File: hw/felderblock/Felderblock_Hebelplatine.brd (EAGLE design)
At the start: 50 x 78 mm, 35 parts, among them IC3 MCP23017SP

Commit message: last check
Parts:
- FS1-5, FS2-6, FS3-7, FS4-8: device Jens:DIL6_LARGE -> Jens:DIL6_LANGLOCH
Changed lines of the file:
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@@
 <attribute name="VALUE" x="30.226" y="5.6388" size="1.27" layer="27" ratio="10" rot="R180"/>
 </element>
-<element name="FS1-5" library="Jens" package="DIL6_LARGE" value="" x="15.24" y="70" smashed="yes">
+<element name="FS1-5" library="Jens" package="DIL6_LANGLOCH" value="" x="15.24" y="70" smashed="yes">
 <attribute name="VALUE" x="10.16" y="61.55" size="1.778" layer="27"/>
 </element>
-<element name="FS2-6" library="Jens" package="DIL6_LARGE" value="" x="15.24" y="50" smashed="yes">
+<element name="FS2-6" library="Jens" package="DIL6_LANGLOCH" value="" x="15.24" y="50" smashed="yes">
 <attribute name="VALUE" x="10.16" y="41.55" size="1.778" layer="27"/>
 </element>
-<element name="FS3-7" library="Jens" package="DIL6_LARGE" value="" x="15.24" y="30" smashed="yes">
+<element name="FS3-7" library="Jens" package="DIL6_LANGLOCH" value="" x="15.24" y="30" smashed="yes">
 <attribute name="VALUE" x="10.16" y="21.55" size="1.778" layer="27"/>
 </element>
-<element name="FS4-8" library="Jens" package="DIL6_LARGE" value="" x="15.24" y="10" smashed="yes">
+<element name="FS4-8" library="Jens" package="DIL6_LANGLOCH" value="" x="15.24" y="10" smashed="yes">
 <attribute name="VALUE" x="10.16" y="1.55" size="1.778" layer="27"/>
 </element>

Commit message: last update for mfg
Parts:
- FS1-5, FS2-6, FS3-7, FS4-8: device Jens:DIL6_LANGLOCH -> Jens:DIL6_LARGE
- LED1, LED2, LED3, LED4, LED5, LED6, LED7, LED8: device SparkFun-LED:LED_3MM -> SparkFun-LED:LED3MM
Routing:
- net +5V: track 182.0 -> 158.7 mm
- net FST7: track 26.9 -> 26.3 mm
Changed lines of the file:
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@@
 <attribute name="VALUE" x="39.7002" y="64.643" size="1.778" layer="27" ratio="10" rot="R270"/>
 </element>
-<element name="LED3" library="SparkFun-LED" package="LED_3MM" value="" x="25.4" y="30" smashed="yes">
-<attribute name="PROD_ID" value="DIO-08794" x="25.4" y="30" size="1.778" layer="27" display="off"/>
+<element name="LED3" library="SparkFun-LED" package="LED3MM" value="" x="25.4" y="30" smashed="yes">
 <attribute name="VALUE" x="25.4" y="27.714" size="0.6096" layer="27" font="vector" ratio="20" align="top-center"/>
 </element>
-<element name="LED8" library="SparkFun-LED" package="LED_3MM" value="" x="5.08" y="10" smashed="yes">
-<attribute name="PROD_ID" value="DIO-08794" x="5.08" y="10" size="1.778" layer="27" display="off"/>
+<element name="LED8" library="SparkFun-LED" package="LED3MM" value="" x="5.08" y="10" smashed="yes">
 <attribute name="VALUE" x="5.08" y="7.714" size="0.6096" layer="27" font="vector" ratio="20" align="top-center"/>
 </element>
-<element name="LED4" library="SparkFun-LED" package="LED_3MM" value="" x="25.4" y="10" smashed="yes">
-<attribute name="PROD_ID" value="DIO-08794" x="25.4" y="10" size="1.778" layer="27" display="off"/>
+<element name="LED4" library="SparkFun-LED" package="LED3MM" value="" x="25.4" y="10" smashed="yes">
 <attribute name="VALUE" x="25.4" y="7.714" size="0.6096" layer="27" font="vector" ratio="20" align="top-center"/>
 </element>
-<element name="LED5" library="SparkFun-LED" package="LED_3MM" value="" x="5.08" y="70" smashed="yes">
-<attribute name="PROD_ID" value="DIO-08794" x="5.08" y="70" size="1.778" layer="27" display="off"/>
+<element name="LED5" library="SparkFun-LED" package="LED3MM" value="" x="5.08" y="70" smashed="yes">
 <attribute name="VALUE" x="5.08" y="67.714" size="0.6096" layer="27" font="vector" ratio="20" align="top-center"/>
 </element>
-<element name="LED1" library="SparkFun-LED" package="LED_3MM" value="" x="25.4" y="70" smashed="yes">
-<attribute name="PROD_ID" value="DIO-08794" x="25.4" y="70" size="1.778" layer="27" display="off"/>
+<element name="LED1" library="SparkFun-LED" package="LED3MM" value="" x="25.4" y="70" smashed="yes">
 <attribute name="VALUE" x="25.4" y="67.714" size="0.6096" layer="27" font="vector" ratio="20" align="top-center"/>
 </element>
-<element name="LED6" library="SparkFun-LED" package="LED_3MM" value="" x="5.08" y="50" smashed="yes">
-<attribute name="PROD_ID" value="DIO-08794" x="5.08" y="50" size="1.778" layer="27" display="off"/>
+<element name="LED6" library="SparkFun-LED" package="LED3MM" value="" x="5.08" y="50" smashed="yes">
 <attribute name="VALUE" x="5.08" y="47.714" size="0.6096" layer="27" font="vector" ratio="20" align="top-center"/>
 </element>
-<element name="LED2" library="SparkFun-LED" package="LED_3MM" value="" x="25.4" y="50" smashed="yes">
-<attribute name="PROD_ID" value="DIO-08794" x="25.4" y="50" size="1.778" layer="27" display="off"/>
+<element name="LED2" library="SparkFun-LED" package="LED3MM" value="" x="25.4" y="50" smashed="yes">
 <attribute name="VALUE" x="25.4" y="47.714" size="0.6096" layer="27" font="vector" ratio="20" align="top-center"/>
 </element>
-<element name="LED7" library="SparkFun-LED" package="LED_3MM" value="" x="5.08" y="30" smashed="yes">
-<attribute name="PROD_ID" value="DIO-08794" x="5.08" y="30" size="1.778" layer="27" display="off"/>
+<element name="LED7" library="SparkFun-LED" package="LED3MM" value="" x="5.08" y="30" smashed="yes">
 <attribute name="VALUE" x="5.08" y="27.714" size="0.6096" layer="27" font="vector" ratio="20" align="top-center"/>
 </element>
@@
 <attribute name="VALUE" x="30.226" y="5.6388" size="1.27" layer="27" ratio="10" rot="R180"/>
 </element>
-<element name="FS1-5" library="Jens" package="DIL6_LANGLOCH" value="" x="15.24" y="70" smashed="yes">
+<element name="FS1-5" library="Jens" package="DIL6_LARGE" value="" x="15.24" y="70" smashed="yes">
 <attribute name="VALUE" x="10.16" y="61.55" size="1.778" layer="27"/>
 </element>
-<element name="FS2-6" library="Jens" package="DIL6_LANGLOCH" value="" x="15.24" y="50" smashed="yes">
+<element name="FS2-6" library="Jens" package="DIL6_LARGE" value="" x="15.24" y="50" smashed="yes">
 <attribute name="VALUE" x="10.16" y="41.55" size="1.778" layer="27"/>
 </element>
-<element name="FS3-7" library="Jens" package="DIL6_LANGLOCH" value="" x="15.24" y="30" smashed="yes">
+<element name="FS3-7" library="Jens" package="DIL6_LARGE" value="" x="15.24" y="30" smashed="yes">
 <attribute name="VALUE" x="10.16" y="21.55" size="1.778" layer="27"/>
 </element>
-<element name="FS4-8" library="Jens" package="DIL6_LANGLOCH" value="" x="15.24" y="10" smashed="yes">
+<element name="FS4-8" library="Jens" package="DIL6_LARGE" value="" x="15.24" y="10" smashed="yes">
 <attribute name="VALUE" x="10.16" y="1.55" size="1.778" layer="27"/>
 </element>
@@
 <wire x1="40.9194" y1="16.4592" x2="41.005" y2="16.425" width="0.254" layer="1"/>
 <wire x1="40.9194" y1="25.146" x2="41.005" y2="25.315" width="0.254" layer="1"/>
-<wire x1="37.2364" y1="12.5476" x2="24.0284" y2="12.5476" width="0.254" layer="1"/>
+<wire x1="37.2364" y1="12.5476" x2="24.6634" y2="12.5476" width="0.254" layer="1"/>
 <wire x1="40.9194" y1="16.2306" x2="37.2364" y2="12.5476" width="0.254" layer="1"/>
 <wire x1="40.9194" y1="16.2306" x2="41.005" y2="16.425" width="0.254" layer="1"/>
 <wire x1="40.9194" y1="42.5958" x2="38.4302" y2="45.085" width="0.6096" layer="1"/>
 <wire x1="38.4302" y1="45.085" x2="36.83" y2="45.085" width="0.6096" layer="1"/>
-<wire x1="24.0284" y1="12.5476" x2="24.0284" y2="11.9634" width="0.3048" layer="1"/>
+<wire x1="24.6634" y1="12.5476" x2="24.0284" y2="11.9634" width="0.3048" layer="1"/>
 <wire x1="24.0284" y1="11.9634" x2="22.225" y2="10.16" width="0.3048" layer="1"/>
-<wire x1="22.225" y1="10.16" x2="17.145" y2="10.16" width="0.3048" layer="1"/>
-<wire x1="15.24" y1="72.4" x2="15.24" y2="73.66" width="0.3048" layer="1"/>
-<wire x1="15.24" y1="73.66" x2="17.145" y2="75.565" width="0.3048" layer="1"/>
-<wire x1="17.145" y1="75.565" x2="25.4" y2="75.565" width="0.3048" layer="1"/>
-<wire x1="25.4" y1="75.565" x2="26.035" y2="74.93" width="0.3048" layer="1"/>
-<wire x1="26.035" y1="74.93" x2="26.035" y2="73.66" width="0.3048" layer="1"/>
-<wire x1="26.035" y1="73.66" x2="25.4" y2="73.025" width="0.3048" layer="1"/>
-<wire x1="25.4" y1="73.025" x2="23.495" y2="73.025" width="0.3048" layer="1"/>
-<wire x1="23.495" y1="73.025" x2="22.225" y2="71.755" width="0.3048" layer="1"/>
-<wire x1="22.225" y1="71.755" x2="22.225" y2="64.77" width="0.3048" layer="1"/>
-<wire x1="22.225" y1="64.77" x2="20.955" y2="63.5" width="0.3048" layer="1"/>
-<wire x1="20.955" y1="63.5" x2="15.875" y2="63.5" width="0.3048" layer="1"/>
-<wire x1="15.875" y1="63.5" x2="8.255" y2="55.88" width="0.3048" layer="1"/>
+<wire x1="17.78" y1="65.405" x2="8.255" y2="55.88" width="0.3048" layer="1"/>
 <wire x1="15.24" y1="52.4" x2="15.24" y2="51.435" width="0.3048" layer="1"/>
 <wire x1="15.24" y1="51.435" x2="13.97" y2="50.165" width="0.3048" layer="1"/>
@@
 <wire x1="15.24" y1="34.925" x2="15.24" y2="32.4" width="0.3048" layer="1"/>
 <wire x1="15.24" y1="12.4" x2="15.24" y2="12.065" width="0.3048" layer="1"/>
-<wire x1="15.24" y1="12.065" x2="17.145" y2="10.16" width="0.3048" layer="1"/>
-<wire x1="17.145" y1="10.16" x2="8.255" y2="10.16" width="0.3048" layer="1"/>
+<wire x1="22.225" y1="10.16" x2="15.24" y2="10.16" width="0.3048" layer="1"/>
+<wire x1="15.24" y1="10.16" x2="8.255" y2="10.16" width="0.3048" layer="1"/>
 <wire x1="8.255" y1="10.16" x2="7.62" y2="10.795" width="0.3048" layer="1"/>
 <wire x1="7.62" y1="10.795" x2="7.62" y2="13.335" width="0.3048" layer="1"/>
@@
 <wire x1="12.7" y1="21.59" x2="8.255" y2="26.035" width="0.3048" layer="1"/>
 <wire x1="8.255" y1="26.035" x2="8.255" y2="35.56" width="0.3048" layer="1"/>
+<wire x1="15.24" y1="12.065" x2="15.24" y2="10.16" width="0.4064" layer="1"/>
+<wire x1="17.79" y1="69.85" x2="15.24" y2="72.4" width="0.3048" layer="1"/>
+<wire x1="17.78" y1="65.405" x2="17.78" y2="69.84" width="0.3048" layer="1"/>
+<wire x1="17.78" y1="69.84" x2="17.79" y2="69.85" width="0.3048" layer="1"/>
 </signal>
 <signal name="FST1">
@@
 <wire x1="35.8902" y1="50.0634" x2="36.8046" y2="50.0634" width="0.254" layer="16"/>
 <wire x1="33.3756" y1="47.5488" x2="35.8902" y2="50.0634" width="0.254" layer="16"/>
-<wire x1="33.3756" y1="44.3484" x2="33.3756" y2="47.5488" width="0.254" layer="16"/>
+<wire x1="33.3756" y1="45.6184" x2="33.3756" y2="47.5488" width="0.254" layer="16"/>
 <wire x1="36.8046" y1="50.0634" x2="36.83" y2="50.165" width="0.254" layer="16"/>
 <wire x1="22.5158" y1="34.9758" x2="19.94" y2="32.4" width="0.3048" layer="1"/>
-<wire x1="33.3756" y1="44.3484" x2="32.2834" y2="44.3484" width="0.3048" layer="16"/>
+<wire x1="33.3756" y1="45.6184" x2="32.2834" y2="44.3484" width="0.3048" layer="16"/>
 <wire x1="32.2834" y1="44.3484" x2="24.13" y2="36.195" width="0.3048" layer="16"/>
 <wire x1="24.13" y1="36.195" x2="24.13" y2="34.925" width="0.3048" layer="16"/>
@@
 <wire x1="47.3202" y1="66.0654" x2="47.3202" y2="58.293" width="0.254" layer="1"/>
 <wire x1="45.9486" y1="67.437" x2="47.3202" y2="66.0654" width="0.254" layer="1"/>
-<wire x1="26.9748" y1="67.437" x2="45.9486" y2="67.437" width="0.254" layer="1"/>
-<wire x1="21.9456" y1="62.4078" x2="26.9748" y2="67.437" width="0.254" layer="1"/>
-<wire x1="17.8308" y1="62.4078" x2="21.9456" y2="62.4078" width="0.254" layer="1"/>
+<wire x1="27.6098" y1="67.437" x2="45.9486" y2="67.437" width="0.254" layer="1"/>
+<wire x1="22.5806" y1="62.4078" x2="27.6098" y2="67.437" width="0.254" layer="1"/>
+<wire x1="17.8308" y1="62.4078" x2="22.5806" y2="62.4078" width="0.254" layer="1"/>
 <wire x1="44.577" y1="57.8358" x2="44.45" y2="57.785" width="0.254" layer="1"/>
 <wire x1="17.8308" y1="62.4078" x2="17.78" y2="62.23" width="0.254" layer="1"/>

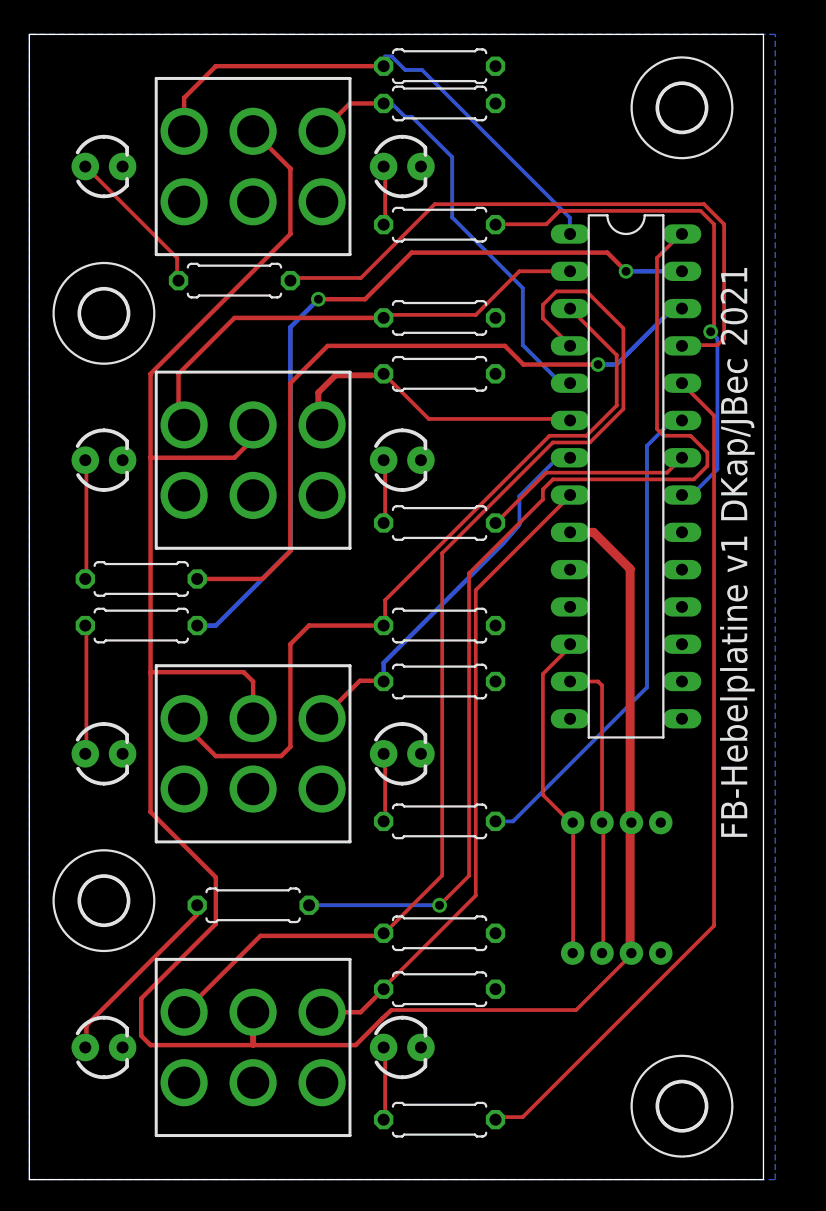
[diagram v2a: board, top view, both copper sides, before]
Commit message: moved components to backside
- Components of main panel moved to backside
-  corrected connections for MCP on Hebelplatine
- added address jumpers on Hebelplatine
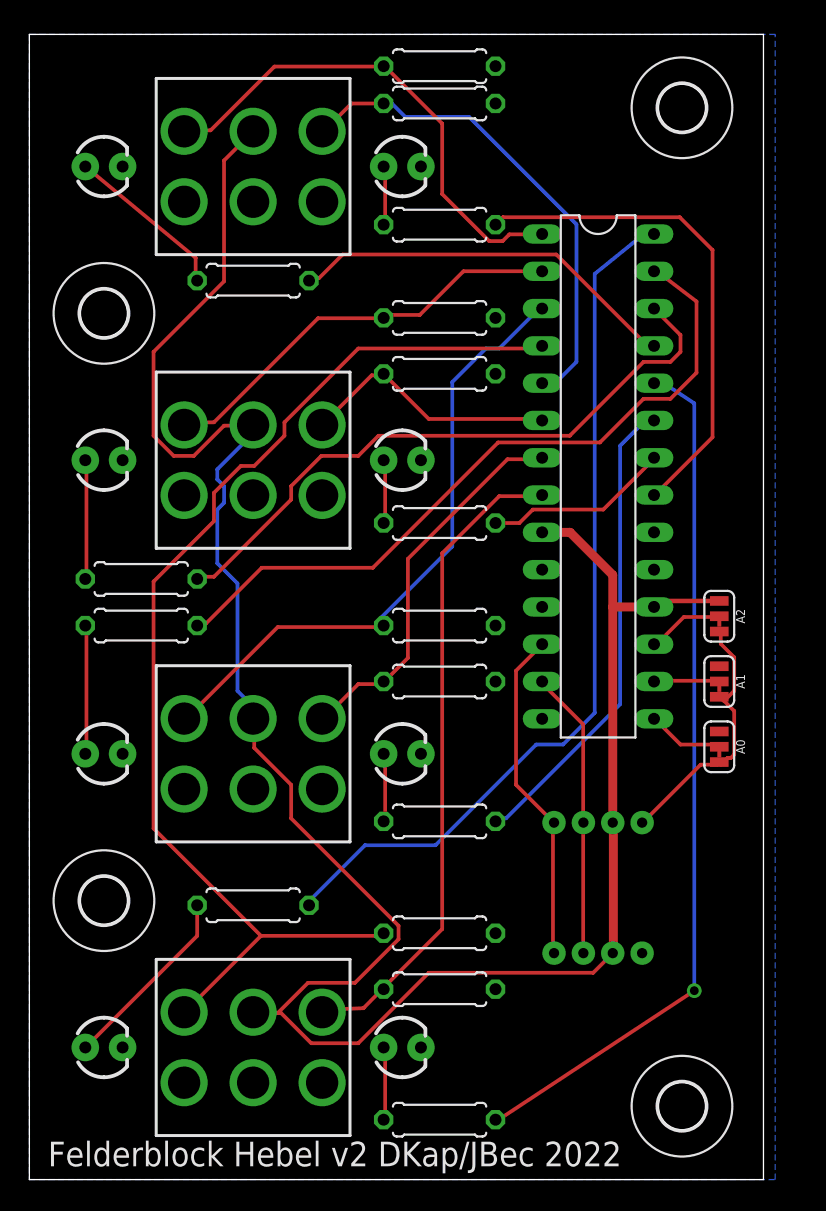
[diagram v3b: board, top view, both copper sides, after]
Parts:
- added A0, A1, A2: (no value), SparkFun-Jumpers:SMT-JUMPER_3_1-NC_TRACE_SILK
- moved IC3 1.91 mm to (38.7, 48.9)
- moved I2C-1 1.27 mm to (38.7, 24.8)
- moved I2C-2 1.27 mm to (38.7, 15.9)
- moved R23 1.27 mm to (15.2, 62.2)
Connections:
- new net N$1: A0.2, IC3.15
- new net N$2: A2.2, IC3.17
- new net N$3: A1.2, IC3.16
- net +5V: now also A0.1, A1.1, A2.1, IC3.18
- net GND: now also A0.3, A1.3, A2.3; no longer IC3.15, IC3.16, IC3.17
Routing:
- net GND: track 0.00 -> 18.6 mm
- net FST5_LED: track 43.2 -> 26.8 mm
- net FST8_LED: track 71.0 -> 59.9 mm, vias 1 -> 0
- net FST3: track 53.6 -> 43.0 mm
- net +5V: track 158.7 -> 150.8 mm
- net N$1: track 0.00 -> 5.23 mm
- net N$2: track 0.00 -> 5.21 mm
- net FST6_LED: track 48.4 -> 43.6 mm, vias 1 -> 0
- net FST2: track 33.2 -> 28.7 mm
- net N$3: track 0.00 -> 4.46 mm
- net FST6: track 21.3 -> 17.7 mm
- net FST5: track 30.3 -> 33.8 mm
- net FST7_LED: track 53.0 -> 49.7 mm, vias 2 -> 0
- net FST4: track 75.8 -> 77.8 mm
- net FST2_LED: track 14.5 -> 12.7 mm
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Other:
- board text added: "Felderblock Hebel v2 DKap/JBec 2022"
- board text removed: "FB-Hebelplatine v1 DKap/JBec 2021"

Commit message: Extended to six fields
Extended to six fields per PCB
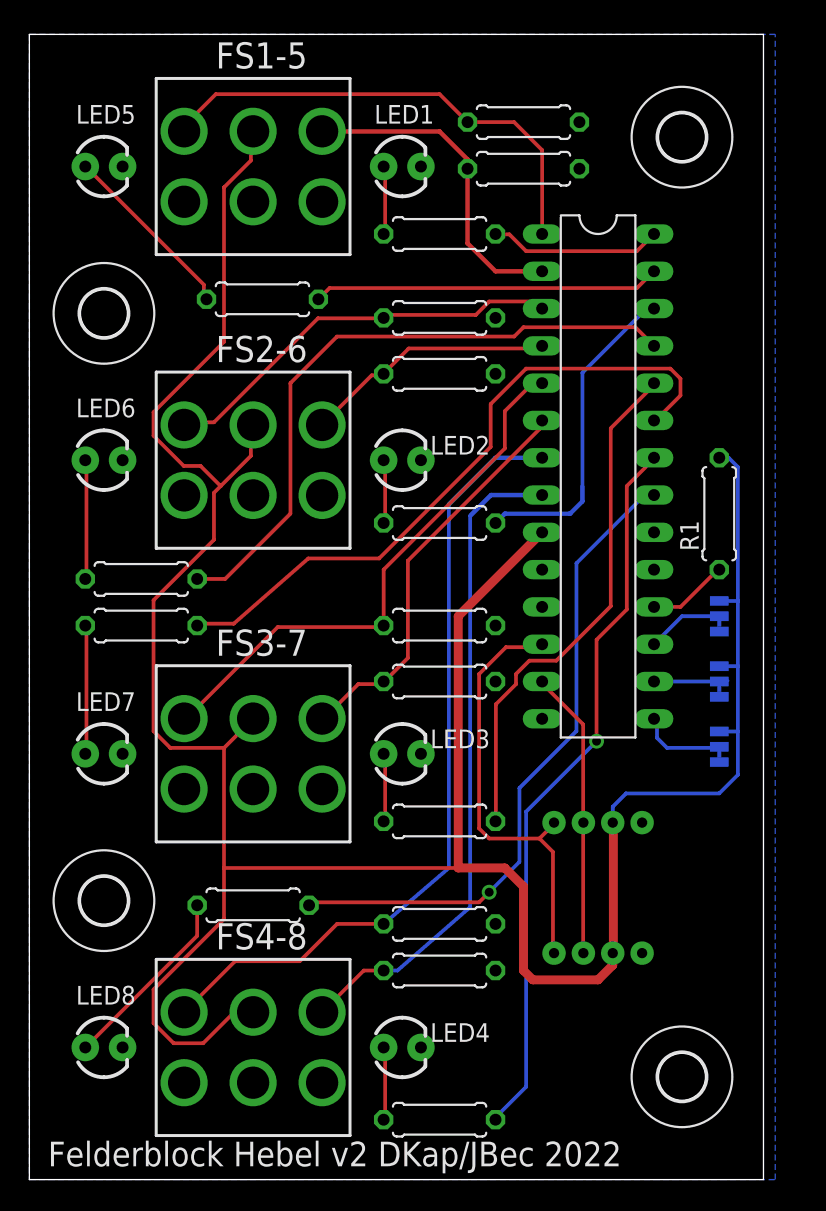
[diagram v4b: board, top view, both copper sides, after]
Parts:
- added R1: 10k, resistor:0207/7
- moved R22 7.24 mm to (33.7, 69.8)
- moved R18 6.87 mm to (33.7, 73.0)
- moved H1 2.00 mm to (44.5, 72.0)
- moved H2 2.00 mm to (44.5, 8.00)
- moved R23 1.42 mm to (15.9, 61.0)
- moved R19 1.27 mm to (27.9, 15.2)
- moved R24 0.64 mm to (27.9, 65.4)
- moved R15 0.63 mm to (27.9, 18.4)
- flipped A0 to the bottom
- flipped A1 to the bottom
- flipped A2 to the bottom
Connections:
- new net N$4: IC3.18, R1.1
- net +5V: now also R1.2; no longer IC3.18
- net FST1_LED: now also IC3.28; no longer IC3.21
- net FST2: now also IC3.3; no longer IC3.2
- net FST2_LED: now also IC3.26; no longer IC3.22
- net FST3: now also IC3.5; no longer IC3.3
- net FST3_LED: now also IC3.24; no longer IC3.23
- net FST4: now also IC3.7; no longer IC3.4
- net FST4_LED: now also IC3.22; no longer IC3.24
- net FST5: now also IC3.2; no longer IC3.5
- net FST5_LED: now also IC3.27; no longer IC3.25
- net FST6: now also IC3.4; no longer IC3.6
- net FST6_LED: now also IC3.25; no longer IC3.26
- net FST7: now also IC3.6; no longer IC3.7
- net FST7_LED: now also IC3.23; no longer IC3.27
- net FST8_LED: now also IC3.21; no longer IC3.28
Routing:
- net +5V: track 150.8 -> 195.7 mm
- net FST4: track 77.8 -> 54.4 mm
- net FST1_LED: track 34.3 -> 11.8 mm
- net GND: track 18.6 -> 0.00 mm
- net FST8_LED: track 59.9 -> 44.8 mm, vias 0 -> 1
- net FST5: track 33.8 -> 22.3 mm
- net FST4_LED: track 59.4 -> 49.5 mm
- net FST2_LED: track 12.7 -> 22.0 mm
- net SCL: track 22.9 -> 29.8 mm
- net N$4: track 0.00 -> 5.49 mm
- net FST3: track 43.0 -> 37.5 mm
- net FST7_LED: track 49.7 -> 45.7 mm
- net FST5_LED: track 26.8 -> 23.6 mm
- net FST3_LED: track 32.6 -> 35.4 mm
- net FST7: track 26.3 -> 27.5 mm
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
